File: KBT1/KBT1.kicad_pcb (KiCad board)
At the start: 2 copper layers, 115.3 x 83.3 mm, 48 parts, among them K0 KEYSW, K1 KEYSW, K10 KEYSW, K11 KEYSW, K12 KEYSW, K13 KEYSW, K14 KEYSW, K15 KEYSW, K2 KEYSW, K3 KEYSW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

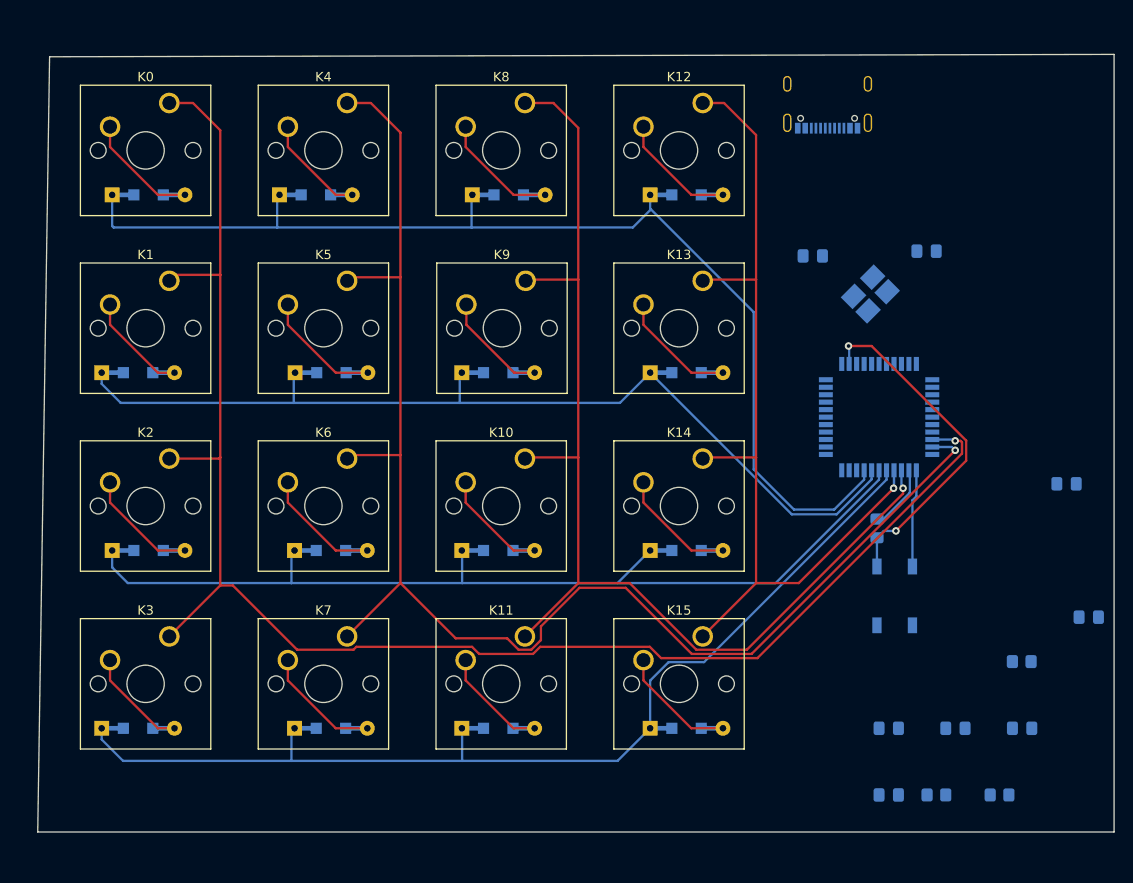
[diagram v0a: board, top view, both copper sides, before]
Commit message: keyboard tester initial work
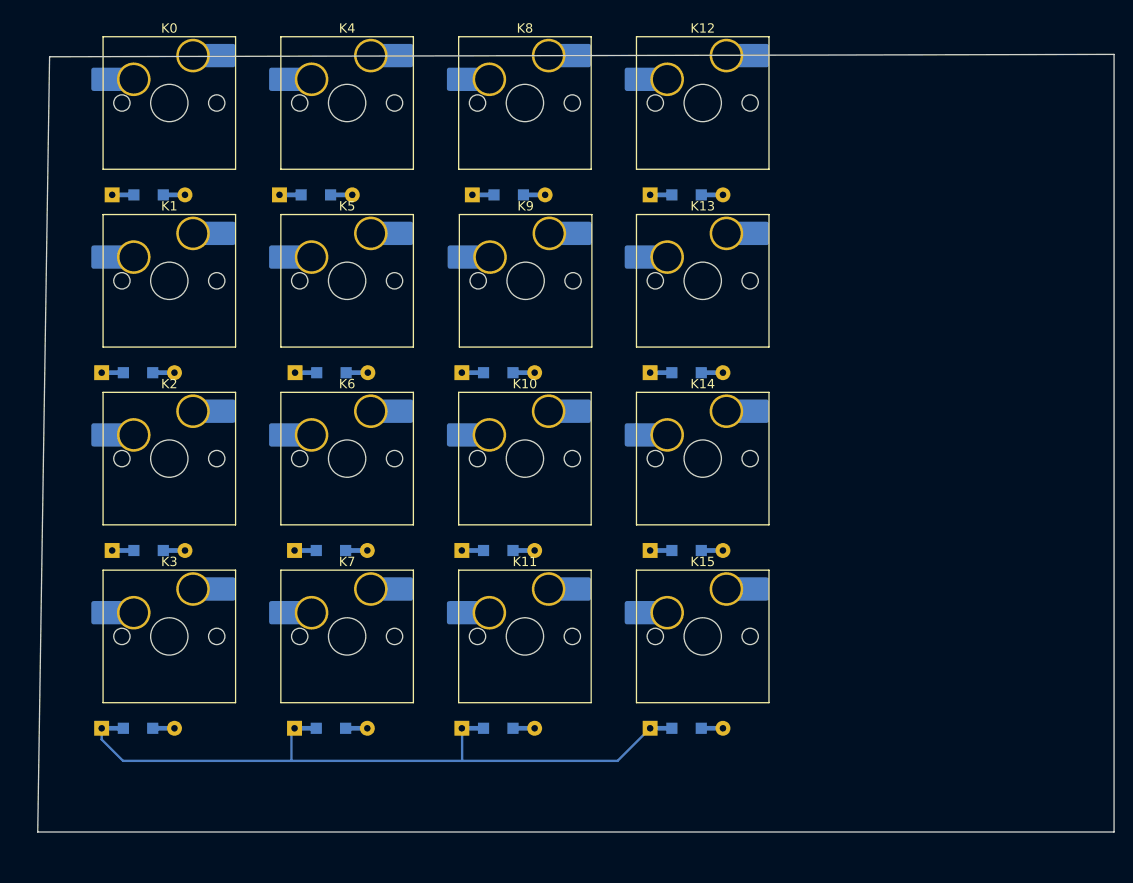
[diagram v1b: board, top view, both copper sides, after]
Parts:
- removed C1, C2, C3, C4: 0.1u, Capacitor_SMD:C_0805_2012Metric_Pad1.18x1.45mm_HandSolder
- removed C5: 4.7u, Capacitor_SMD:C_0805_2012Metric_Pad1.18x1.45mm_HandSolder
- removed C6, C7: 22p, Capacitor_SMD:C_0805_2012Metric_Pad1.18x1.45mm_HandSolder
- removed C8: 1u, Capacitor_SMD:C_0805_2012Metric_Pad1.18x1.45mm_HandSolder
- removed P1: USB_C_Plug_USB2.0, Connector_USB:USB_C_Receptacle_Palconn_UTC16-G
- removed R1, R4: 10k, Resistor_SMD:R_0805_2012Metric_Pad1.20x1.40mm_HandSolder
- removed R2, R3: 22, Resistor_SMD:R_0805_2012Metric_Pad1.20x1.40mm_HandSolder
- removed SW1: SW_PUSH, Button_Switch_SMD:SW_SPST_TL3342
- removed U1: ATMEGA32U4, Package_QFP:TQFP-44_10x10mm_P0.8mm
- removed X1: XTAL_GND, Crystal:Crystal_SMD_SeikoEpson_FA238-4Pin_3.2x2.5mm_HandSoldering
- K0, K1, K10, K11, K12, K13, K14, K15, K2, K3, K4, K5, K6, K7, K8, K9: footprint Button_Switch_Keyboard:SW_Cherry_MX_1.00u_PCB -> 6:SW_Hotswap_Kailh_MX_plated
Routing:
- net /col0: track 171.6 -> 0.00 mm, vias 1 -> 0
- net /col1: track 155.7 -> 0.00 mm, vias 1 -> 0
- net /col2: track 122.4 -> 0.00 mm, vias 1 -> 0
- net /row0: track 119.0 -> 0.00 mm
- net /row2: track 102.3 -> 0.04 mm
- net /row1: track 101.3 -> 0.00 mm
- net /col3: track 95.6 -> 0.00 mm, vias 1 -> 0
- net /row3: track 109.8 -> 69.5 mm
- net Net-(R1-Pad1): track 37.0 -> 0.00 mm, vias 2 -> 0
- net +5V: track 17.6 -> 0.00 mm
- net Net-(D6-Pad2): track 12.9 -> 0.00 mm
- net Net-(D14-Pad2): track 12.8 -> 0.00 mm
- net Net-(D13-Pad2): track 12.8 -> 0.00 mm
- net Net-(D16-Pad2): track 12.8 -> 0.00 mm
- net Net-(D15-Pad2): track 12.8 -> 0.00 mm
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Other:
- net class Default removed

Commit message: increased header size
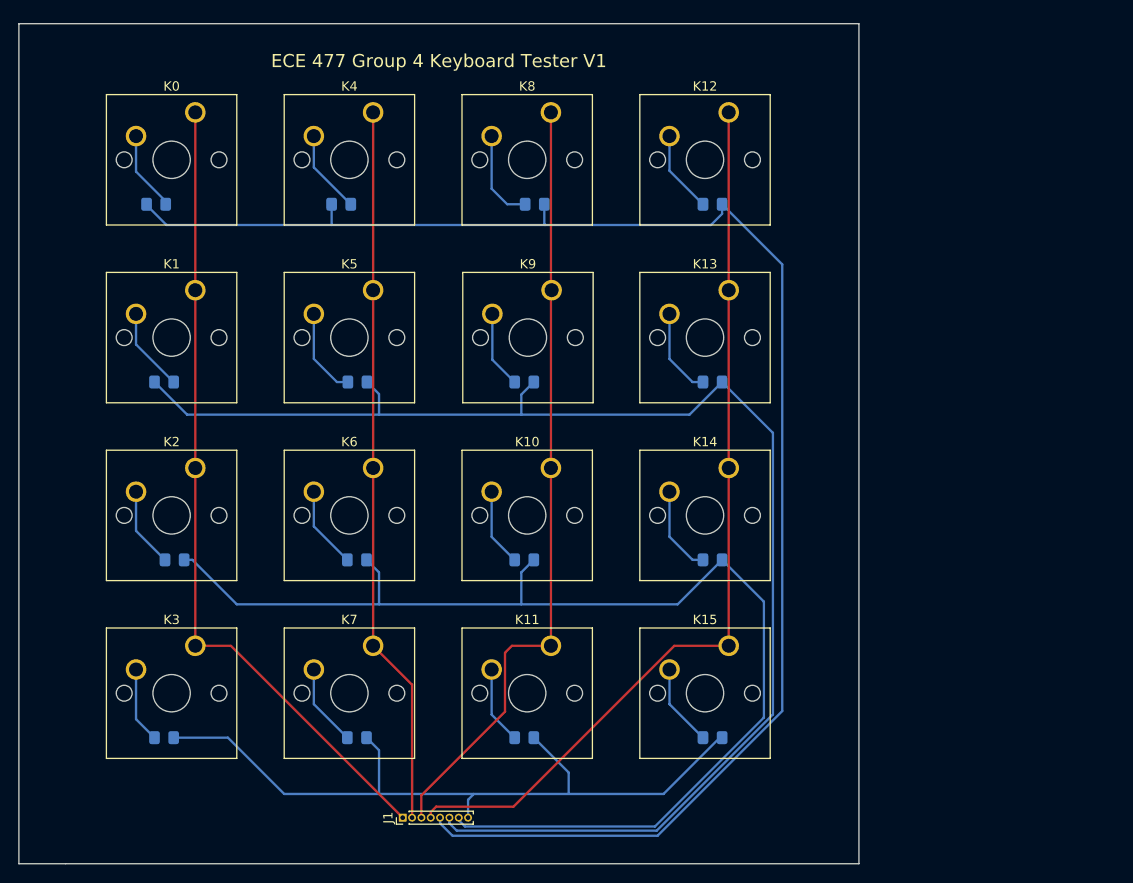
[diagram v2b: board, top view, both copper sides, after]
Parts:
- added J1: Conn_01x08_Male, Connector_PinHeader_1.00mm:PinHeader_1x08_P1.00mm_Vertical, F.Cu at (56.1, 100.1)
- D1, D10, D11, D12, D13, D14, D15, D16, D2, D3, D4, D5, D6, D7, D8, D9: footprint keyboard_parts:D_SOD123_axial -> Diode_SMD:D_0805_2012Metric_Pad1.15x1.40mm_HandSolder
- K0, K1, K10, K11, K12, K13, K14, K15, K2, K3, K4, K5, K6, K7, K8, K9: footprint 6:SW_Hotswap_Kailh_MX_plated -> Button_Switch_Keyboard:SW_Cherry_MX_1.00u_PCB
- moved D8 2.96 mm to (51.2, 91.5), turned to 180 degrees
- moved K7 2.96 mm to (53.0, 81.7)
- moved K6 2.96 mm to (53.0, 62.6)
- moved K4 2.96 mm to (53.0, 24.5)
- moved D4 2.96 mm to (30.6, 91.5), turned to 180 degrees
- moved K3 2.96 mm to (33.9, 81.7)
- moved D6 2.96 mm to (51.3, 53.4), turned to 180 degrees
- moved D7 2.96 mm to (51.2, 72.4), turned to 180 degrees
- moved K5 2.96 mm to (53.0, 43.5)
- moved K2 2.96 mm to (33.9, 62.6)
- moved D12 2.96 mm to (69.1, 91.5), turned to 180 degrees
- moved D16 2.96 mm to (89.3, 91.5), turned to 180 degrees
- moved K0 2.96 mm to (33.9, 24.5)
- moved K11 2.96 mm to (72.0, 81.7)
- moved K15 2.96 mm to (91.0, 81.7)
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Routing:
- net /row0: track 0.00 -> 169.0 mm
- net /row1: track 0.00 -> 150.4 mm
- net /row2: track 0.04 -> 129.0 mm
- net /col3: track 0.00 -> 98.0 mm
- net /col0: track 0.00 -> 87.0 mm
- net /col2: track 0.00 -> 83.8 mm
- net /col1: track 0.00 -> 77.3 mm
- net /row3: track 69.5 -> 80.7 mm
- net Net-(D9-Pad2): track 0.00 -> 9.92 mm
- net Net-(D5-Pad2): track 0.00 -> 9.84 mm
- net Net-(D6-Pad2): track 0.00 -> 9.50 mm
- net Net-(D15-Pad2): track 0.00 -> 9.44 mm
- net Net-(D14-Pad2): track 0.00 -> 9.44 mm
- net Net-(D2-Pad2): track 0.00 -> 8.97 mm
- net Net-(D16-Pad2): track 0.00 -> 8.79 mm
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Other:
- board size 115.3 x 83.3 mm -> 90 x 90 mm
- board text added: "ECE 477 Group 4 Keyboard Tester V1"

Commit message: updated
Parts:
- J1: footprint Connector_PinHeader_1.00mm:PinHeader_1x08_P1.00mm_Vertical -> Connector_PinHeader_2.54mm:PinHeader_1x08_P2.54mm_Vertical
- K0, K1, K10, K11, K12, K13, K14, K15, K2, K3, K4, K5, K6, K7, K8, K9: footprint Button_Switch_Keyboard:SW_Cherry_MX_1.00u_PCB -> 6:SW_Hotswap_Kailh_MX_plated
- moved J1 5.42 mm to (50.8, 99.1)
- moved K10 5.18 mm to (69.8, 67.3)
- moved K4 5.18 mm to (50.8, 29.2)
- moved K5 5.18 mm to (50.8, 48.3)
- moved K6 5.18 mm to (50.8, 67.3)
- moved K8 5.18 mm to (69.8, 29.2)
- moved K9 5.18 mm to (69.9, 48.3)
- moved K0 5.18 mm to (31.8, 29.2)
- moved K1 5.18 mm to (31.8, 48.3)
- moved K2 5.18 mm to (31.8, 67.3)
- moved K12 5.18 mm to (88.9, 29.2)
- moved K13 5.18 mm to (88.9, 48.3)
- moved K14 5.18 mm to (88.9, 67.3)
- moved K11 5.18 mm to (69.8, 86.4)
- moved K7 5.18 mm to (50.8, 86.4)
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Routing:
- net /row0: track 169.0 -> 182.3 mm
- net /row1: track 150.4 -> 159.0 mm
- net /col3: track 98.0 -> 90.1 mm
- net /row3: track 80.7 -> 73.2 mm
- net /col0: track 87.0 -> 94.1 mm
- net /col2: track 83.8 -> 76.7 mm
- net /row2: track 129.0 -> 135.6 mm
- net Net-(D4-Pad2): track 8.12 -> 12.5 mm
- net Net-(D11-Pad2): track 8.32 -> 12.3 mm
- net Net-(D12-Pad2): track 8.32 -> 12.3 mm
- net Net-(D3-Pad2): track 8.59 -> 12.0 mm
- net Net-(D1-Pad2): track 8.62 -> 11.7 mm
- net Net-(D7-Pad2): track 8.79 -> 11.8 mm
- net Net-(D8-Pad2): track 8.79 -> 11.8 mm
- net Net-(D16-Pad2): track 8.79 -> 11.8 mm
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
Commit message: new diode footprint, added mounting holes
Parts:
- added H1: MountingHole, MountingHole:MountingHole_2.7mm, F.Cu at (21.0, 21.0)
- added H2: MountingHole, MountingHole:MountingHole_2.7mm, F.Cu at (99.0, 21.0)
- added H3: MountingHole, MountingHole:MountingHole_2.7mm, F.Cu at (21.0, 99.0)
- added H4: MountingHole, MountingHole:MountingHole_2.7mm, F.Cu at (99.0, 99.0)
- D1, D10, D11, D12, D13, D14, D15, D16, D2, D3, D4, D5, D6, D7, D8, D9: footprint Diode_SMD:D_0805_2012Metric_Pad1.15x1.40mm_HandSolder -> Diode_THT:D_DO-35_SOD27_P7.62mm_Horizontal
- moved D6 2.51 mm to (48.8, 53.6)
- moved D14 2.46 mm to (86.9, 53.6)
- moved D13 2.46 mm to (86.9, 34.5)
- moved D9 2.46 mm to (67.8, 34.5)
- moved D10 1.34 mm to (67.8, 53.6)
- moved D4 0.93 mm to (29.7, 91.7)
- moved D2 0.86 mm to (29.7, 53.6)
- moved D5 0.79 mm to (48.8, 34.5)
- moved D15 0.76 mm to (86.9, 72.6)
- moved D16 0.76 mm to (86.9, 91.7)
- moved D7 0.76 mm to (48.8, 72.6)
- moved D8 0.76 mm to (48.8, 91.7)
- moved D11 0.48 mm to (67.8, 72.6)
- moved D12 0.48 mm to (67.8, 91.7)
- moved D3 0.34 mm to (29.7, 72.6)
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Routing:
- net /row1: track 159.0 -> 152.2 mm
- net /row0: track 182.3 -> 176.9 mm
- net /row2: track 135.6 -> 131.0 mm
- net /col3: track 90.1 -> 92.2 mm
- net /row3: track 73.2 -> 71.5 mm
- net /col0: track 94.1 -> 92.6 mm
- net Net-(D14-Pad2): track 10.7 -> 11.7 mm
- net Net-(D13-Pad2): track 10.7 -> 11.7 mm
- net Net-(D6-Pad2): track 10.7 -> 11.7 mm
- net Net-(D9-Pad2): track 10.8 -> 11.7 mm
- net Net-(D4-Pad2): track 12.5 -> 11.7 mm
- net Net-(D12-Pad2): track 12.3 -> 11.7 mm
- net Net-(D11-Pad2): track 12.3 -> 11.7 mm
